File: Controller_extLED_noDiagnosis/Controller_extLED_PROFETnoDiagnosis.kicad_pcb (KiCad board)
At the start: 2 copper layers, 75 x 60 mm, 13 parts, among them J1 BAT, J2 Switch, J3 RJ12, J4 RJ12, U1 Arduino_Nano_v3.x, U2 BTS

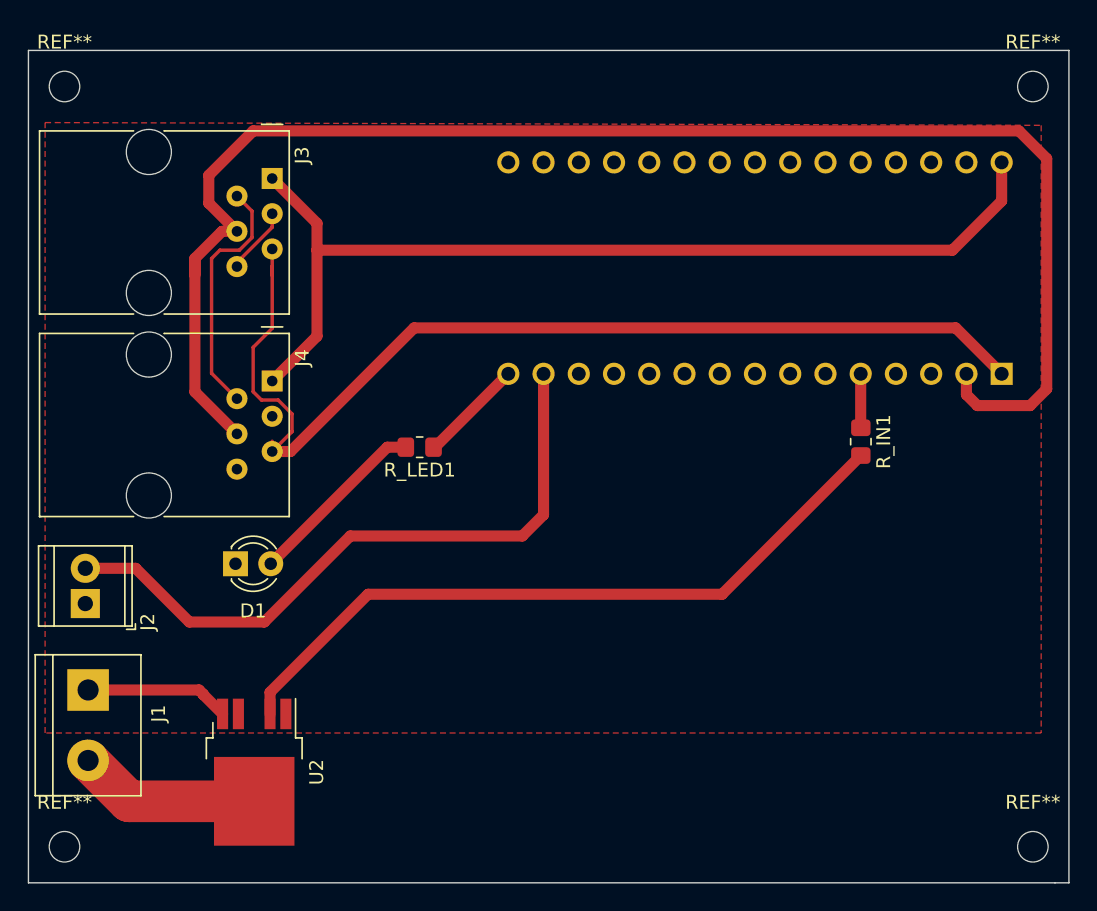
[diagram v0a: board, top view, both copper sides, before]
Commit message: meved pull-up
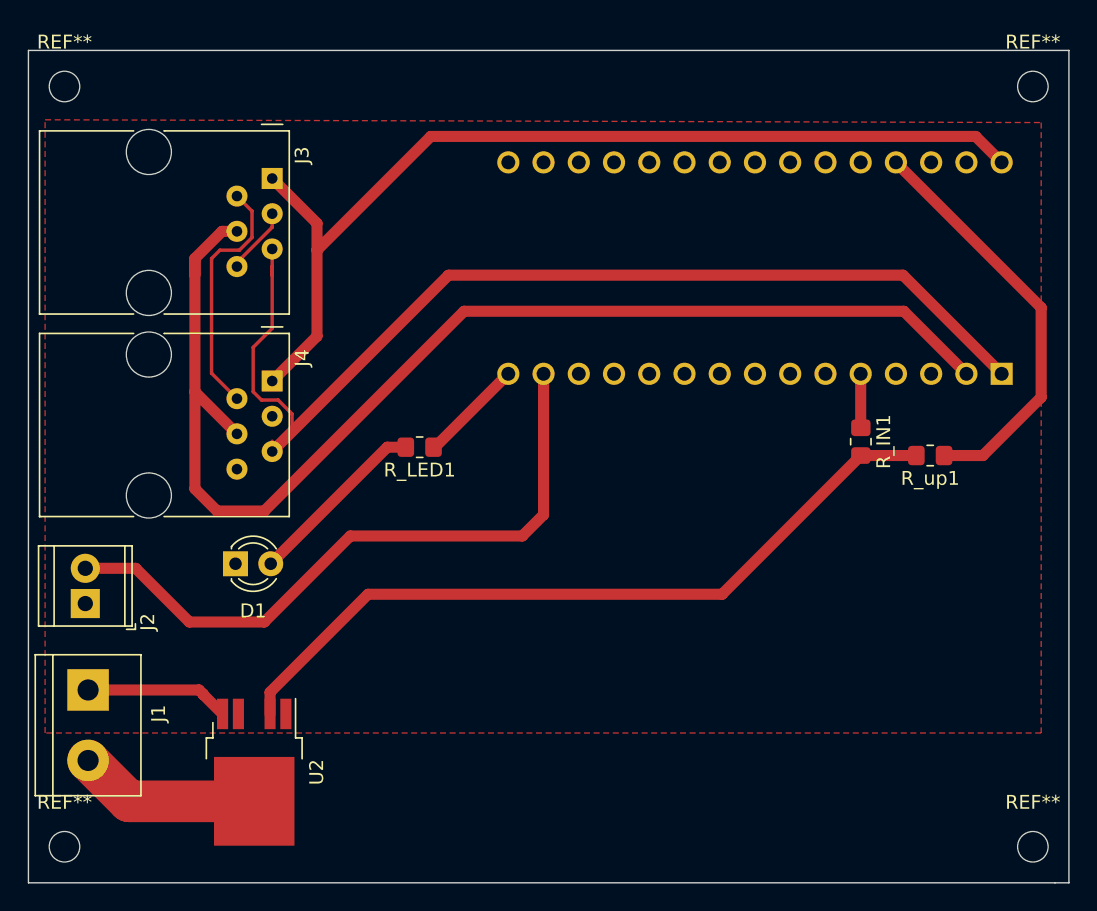
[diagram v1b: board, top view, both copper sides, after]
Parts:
- added R_up1: 4.7k, Resistor_SMD:R_0805_2012Metric_Pad1.20x1.40mm_HandSolder, F.Cu at (203.0, 105.4)
- U2: value BTS -> BTS462T
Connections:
- U1 pad 7: (no net) -> unconnected-(U1-Pad7)
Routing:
- net +5V: track 0.00 -> 30.0 mm
- net /RX: track 111.4 -> 90.3 mm
- net Net-(R_IN1-Pad2): track 51.2 -> 55.2 mm
- net /TX: track 76.7 -> 79.8 mm
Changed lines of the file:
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@@
     )
   )
+  (footprint "Resistor_SMD:R_0805_2012Metric_Pad1.20x1.40mm_HandSolder" (layer "F.Cu")
+    (at 203 105.4 180)
+    (descr "Resistor SMD 0805 (2012 Metric), square (rectangular) end terminal, IPC_7351 nominal with elongated pad for handsoldering. (Body size source: IPC-SM-782 page 72, https://www.pcb-3d.com/wordpress/wp-content/uploads/ipc-sm-782a_amendment_1_and_2.pdf), generated with kicad-footprint-generator")
+    (tags "resistor handsolder")
+    (property "Sheetfile" "Haubenblitzer_v2.kicad_sch")
+    (property "Sheetname" "")
+    (attr smd)
+    (fp_text reference "R_up1" (at 0 -1.65) (layer "F.SilkS")
+      (effects (font (size 1 1) (thickness 0.15)))
+    )
+    (fp_text value "4.7k" (at 0 1.65) (layer "F.Fab")
+      (effects (font (size 1 1) (thickness 0.15)))
+    )
+    (fp_text user "${REFERENCE}" (at 0 0) (layer "F.Fab")
+      (effects (font (size 0.5 0.5) (thickness 0.08)))
+    )
+    (fp_line (start -0.227064 -0.735) (end 0.227064 -0.735) (layer "F.SilkS") (width 0.12))
+    (fp_line (start -0.227064 0.735) (end 0.227064 0.735) (layer "F.SilkS") (width 0.12))
+    (fp_line (start 1.85 -0.95) (end 1.85 0.95) (layer "F.CrtYd") (width 0.05))
+    (fp_line (start -1.85 0.95) (end -1.85 -0.95) (layer "F.CrtYd") (width 0.05))
+    (fp_line (start -1.85 -0.95) (end 1.85 -0.95) (layer "F.CrtYd") (width 0.05))
+    (fp_line (start 1.85 0.95) (end -1.85 0.95) (layer "F.CrtYd") (width 0.05))
+    (fp_line (start 1 0.625) (end -1 0.625) (layer "F.Fab") (width 0.1))
+    (fp_line (start -1 0.625) (end -1 -0.625) (layer "F.Fab") (width 0.1))
+    (fp_line (start -1 -0.625) (end 1 -0.625) (layer "F.Fab") (width 0.1))
+    (fp_line (start 1 -0.625) (end 1 0.625) (layer "F.Fab") (width 0.1))
+    (pad "1" smd roundrect (at -1 0 180) (size 1.2 1.4) (layers "F.Cu" "F.Paste" "F.Mask") (roundrect_rratio 0.208333)
+      (net 13 "+5V") (pintype "passive"))
+    (pad "2" smd roundrect (at 1 0 180) (size 1.2 1.4) (layers "F.Cu" "F.Paste" "F.Mask") (roundrect_rratio 0.208333)
+      (net 11 "Net-(R_IN1-Pad2)") (pintype "passive"))
+    (model "${KICAD6_3DMODEL_DIR}/Resistor_SMD.3dshapes/R_0805_2012Metric.wrl"
+      (offset (xyz 0 0 0))
+      (scale (xyz 1 1 1))
+      (rotate (xyz 0 0 0))
+    )
+  )
   (footprint "Connector_RJ:RJ12_Amphenol_54601" (layer "F.Cu")
     (at 155.57 100.03 -90)
@@
       (effects (font (size 1 1) (thickness 0.15)))
     )
-    (fp_text value "BTS" (at 6.575 -0.125 180) (layer "F.Fab")
+    (fp_text value "BTS462T" (at 6.575 -0.125 180) (layer "F.Fab")
       (effects (font (size 1 1) (thickness 0.15)))
     )
@@
       (net 15 "unconnected-(U1-Pad6)") (pinfunction "D3") (pintype "bidirectional+no_connect"))
     (pad "7" thru_hole oval (at 0 -15.24 90) (size 1.6 1.6) (drill 1) (layers *.Cu *.Mask)
-      (pinfunction "D4") (pintype "bidirectional"))
+      (net 16 "unconnected-(U1-Pad7)") (pinfunction "D4") (pintype "bidirectional+no_connect"))
     (pad "8" thru_hole oval (at 0 -17.78 90) (size 1.6 1.6) (drill 1) (layers *.Cu *.Mask)
       (net 17 "unconnected-(U1-Pad8)") (pinfunction "D5") (pintype "bidirectional+no_connect"))
@@
   (segment (start 149.6 117.4) (end 145.73 113.53) (width 0.8) (layer "F.Cu") (net 5))
   (segment (start 173.6 111.2) (end 161.2 111.2) (width 0.8) (layer "F.Cu") (net 5))
+  (segment (start 158.8 90.6) (end 167 82.4) (width 0.8) (layer "F.Cu") (net 6))
   (segment (start 158.8 90.6) (end 158.8 96.8) (width 0.8) (layer "F.Cu") (net 6))
-  (segment (start 208.15 87.05) (end 208.15 84.27) (width 0.8) (layer "F.Cu") (net 6))
+  (segment (start 167 82.4) (end 206.28 82.4) (width 0.8) (layer "F.Cu") (net 6))
   (segment (start 158.8 96.8) (end 155.57 100.03) (width 0.8) (layer "F.Cu") (net 6))
-  (segment (start 158.8 90.6) (end 204.6 90.6) (width 0.8) (layer "F.Cu") (net 6))
   (segment (start 155.57 85.43) (end 158.8 88.66) (width 0.8) (layer "F.Cu") (net 6))
+  (segment (start 206.28 82.4) (end 208.15 84.27) (width 0.8) (layer "F.Cu") (net 6))
   (segment (start 158.8 88.66) (end 158.8 90.6) (width 0.8) (layer "F.Cu") (net 6))
-  (segment (start 204.6 90.6) (end 208.15 87.05) (width 0.8) (layer "F.Cu") (net 6))
   (segment (start 151.2 99.47) (end 153.03 101.3) (width 0.25) (layer "F.Cu") (net 7))
   (segment (start 153.203731 90.6) (end 151.8 90.6) (width 0.25) (layer "F.Cu") (net 7))
@@
   (segment (start 151.2 91.2) (end 151.2 99.47) (width 0.25) (layer "F.Cu") (net 7))
   (segment (start 153.03 86.7) (end 154.114511 87.784511) (width 0.25) (layer "F.Cu") (net 7))
+  (segment (start 205.61 99.51) (end 201.1 95) (width 0.8) (layer "F.Cu") (net 8))
+  (segment (start 155 109.4) (end 151.6 109.4) (width 0.8) (layer "F.Cu") (net 8))
+  (segment (start 151.6 109.4) (end 150 107.8) (width 0.8) (layer "F.Cu") (net 8))
   (segment (start 150 91.195198) (end 150 92.4) (width 0.8) (layer "F.Cu") (net 8))
-  (segment (start 151 87.21) (end 151 85.2) (width 0.8) (layer "F.Cu") (net 8))
   (segment (start 153.03 103.84) (end 153.03 104.103731) (width 0.25) (layer "F.Cu") (net 8))
-  (segment (start 209.4 82) (end 211.4 84) (width 0.8) (layer "F.Cu") (net 8))
-  (segment (start 151 85.2) (end 154.2 82) (width 0.8) (layer "F.Cu") (net 8))
+  (segment (start 201.1 95) (end 169.4 95) (width 0.8) (layer "F.Cu") (net 8))
   (segment (start 153.03 103.84) (end 150 100.81) (width 0.8) (layer "F.Cu") (net 8))
   (segment (start 151.955198 89.24) (end 150 91.195198) (width 0.8) (layer "F.Cu") (net 8))
   (segment (start 153.03 89.24) (end 151.955198 89.24) (width 0.8) (layer "F.Cu") (net 8))
-  (segment (start 211.4 84) (end 211.4 100.6) (width 0.8) (layer "F.Cu") (net 8))
-  (segment (start 206.4 101.8) (end 205.61 101.01) (width 0.8) (layer "F.Cu") (net 8))
-  (segment (start 154.2 82) (end 209.4 82) (width 0.8) (layer "F.Cu") (net 8))
-  (segment (start 205.61 101.01) (end 205.61 99.51) (width 0.8) (layer "F.Cu") (net 8))
+  (segment (start 169.4 95) (end 155 109.4) (width 0.8) (layer "F.Cu") (net 8))
   (segment (start 150 100.81) (end 150 91.195198) (width 0.8) (layer "F.Cu") (net 8))
-  (segment (start 210.2 101.8) (end 206.4 101.8) (width 0.8) (layer "F.Cu") (net 8))
-  (segment (start 153.03 89.24) (end 151 87.21) (width 0.8) (layer "F.Cu") (net 8))
-  (segment (start 211.4 100.6) (end 210.2 101.8) (width 0.8) (layer "F.Cu") (net 8))
+  (segment (start 150 107.8) (end 150 100.81) (width 0.8) (layer "F.Cu") (net 8))
   (segment (start 156 101.4) (end 154.8 101.4) (width 0.25) (layer "F.Cu") (net 9))
-  (segment (start 204.84 96.2) (end 208.15 99.51) (width 0.8) (layer "F.Cu") (net 9))
+  (segment (start 201.04 92.4) (end 168.28 92.4) (width 0.8) (layer "F.Cu") (net 9))
   (segment (start 155.57 90.51) (end 155.57 91.77) (width 0.25) (layer "F.Cu") (net 9))
   (segment (start 155.57 91.77) (end 155.57 92.43) (width 0.25) (layer "F.Cu") (net 9))
+  (segment (start 168.28 92.4) (end 155.57 105.11) (width 0.8) (layer "F.Cu") (net 9))
   (segment (start 155.57 105.11) (end 157 103.68) (width 0.25) (layer "F.Cu") (net 9))
   (segment (start 155.57 96.23) (end 155.57 91.77) (width 0.25) (layer "F.Cu") (net 9))
-  (segment (start 156.89 105.11) (end 165.8 96.2) (width 0.8) (layer "F.Cu") (net 9))
-  (segment (start 165.8 96.2) (end 204.84 96.2) (width 0.8) (layer "F.Cu") (net 9))
+  (segment (start 208.15 99.51) (end 201.04 92.4) (width 0.8) (layer "F.Cu") (net 9))
   (segment (start 154.2 100.8) (end 154.2 97.6) (width 0.25) (layer "F.Cu") (net 9))
   (segment (start 157 103.68) (end 157 102.4) (width 0.25) (layer "F.Cu") (net 9))
   (segment (start 154.2 97.6) (end 155.57 96.23) (width 0.25) (layer "F.Cu") (net 9))
   (segment (start 157 102.4) (end 156 101.4) (width 0.25) (layer "F.Cu") (net 9))
-  (segment (start 155.57 105.11) (end 156.89 105.11) (width 0.8) (layer "F.Cu") (net 9))
   (segment (start 154.8 101.4) (end 154.2 100.8) (width 0.25) (layer "F.Cu") (net 9))
   (segment (start 155.57 104.37) (end 155.57 105.11) (width 0.25) (layer "F.Cu") (net 9))
@@
   (segment (start 198 105.4) (end 188 115.4) (width 0.8) (layer "F.Cu") (net 11))
   (segment (start 188 115.4) (end 162.480978 115.4) (width 0.8) (layer "F.Cu") (net 11))
+  (segment (start 198 105.4) (end 202 105.4) (width 0.8) (layer "F.Cu") (net 11))
   (segment (start 155.415 122.465978) (end 155.415 124.025) (width 0.8) (layer "F.Cu") (net 11))
   (segment (start 162.480978 115.4) (end 155.415 122.465978) (width 0.8) (layer "F.Cu") (net 11))
   (segment (start 167.3 104.8) (end 172.59 99.51) (width 0.8) (layer "F.Cu") (net 12))
   (segment (start 167.2 104.8) (end 167.3 104.8) (width 0.8) (layer "F.Cu") (net 12))
+  (segment (start 204 105.4) (end 206.8 105.4) (width 0.8) (layer "F.Cu") (net 13))
+  (segment (start 211 94.74) (end 200.53 84.27) (width 0.8) (layer "F.Cu") (net 13))
+  (segment (start 211 101.2) (end 211 94.74) (width 0.8) (layer "F.Cu") (net 13))
+  (segment (start 206.8 105.4) (end 211 101.2) (width 0.8) (layer "F.Cu") (net 13))
   (segment (start 193 99.6) (end 192.91 99.51) (width 0.8) (layer "F.Cu") (net 16))
   (zone (net 1) (net_name "GNDA") (layer "F.Cu") (hatch edge 0.508)
@@
     (polygon
       (pts
-        (xy 211 81.6)
+        (xy 211.000558 81.400002)
         (xy 211 125.4)
         (xy 139.2 125.4)
-        (xy 139.2 81.4)
+        (xy 139.200558 81.200002)
       )
     )
